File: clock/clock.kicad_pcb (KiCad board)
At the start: 2 copper layers, 176.8 x 81.3 mm, 285 parts, among them P101 CONN_01X03, P102 CONN_FAN_PWM, P103 XG4A-1631, P301 MCRF, Q201 MMBT3904, U201 PCA9306, U202 DAC8830, U203 LMV722, U204 LTC2990, U205 LP3853, U206 NC7SZ125, U207 NC7SZ125, U301 Adafruit746, U302 MIC5225, U303 PA6H, U401 74LVC541, U501 TPS56428, U502 TPS56428, U503 TPS56428, U601 ADT7410, U602 DS3231, U603 ADT7410, Y201 FVXO-HC53, Y202 CX210

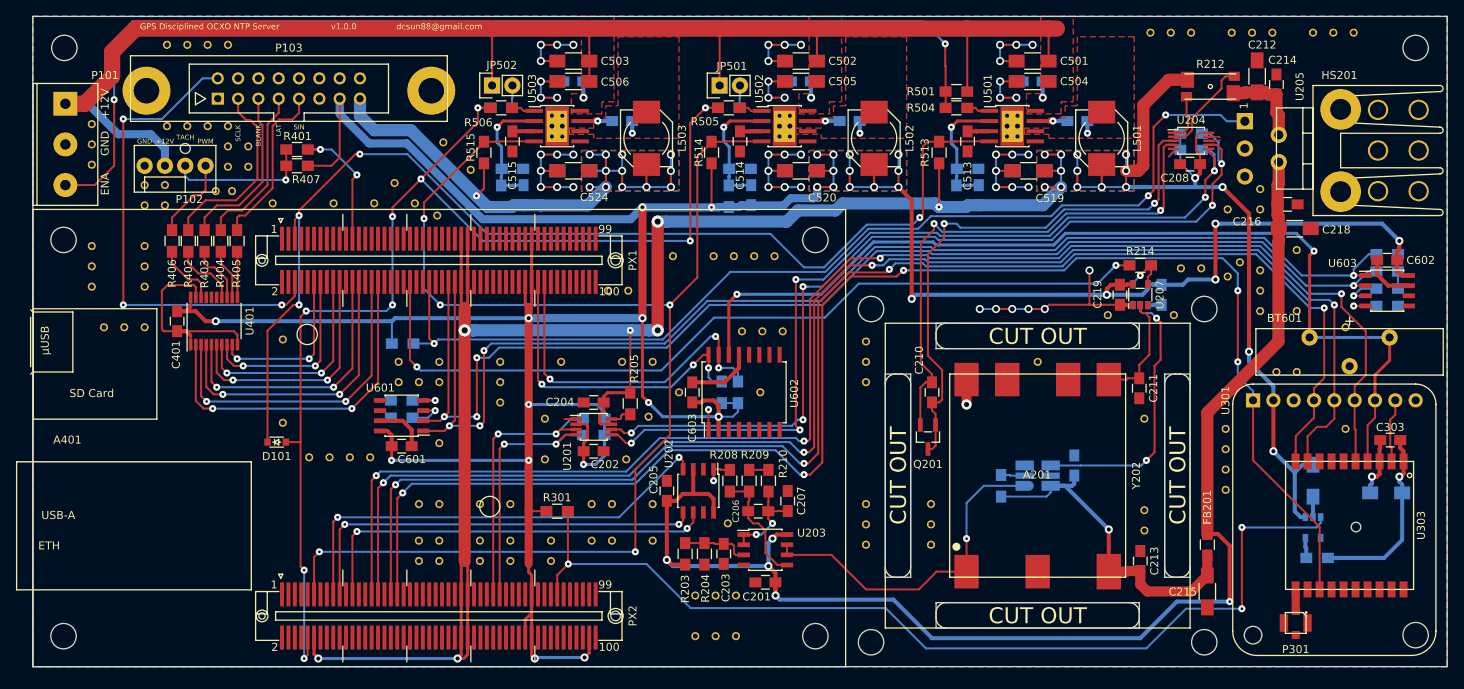
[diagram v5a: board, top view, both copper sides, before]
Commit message: Hide value in stitching via. Reduce width of display board by 10 mils.
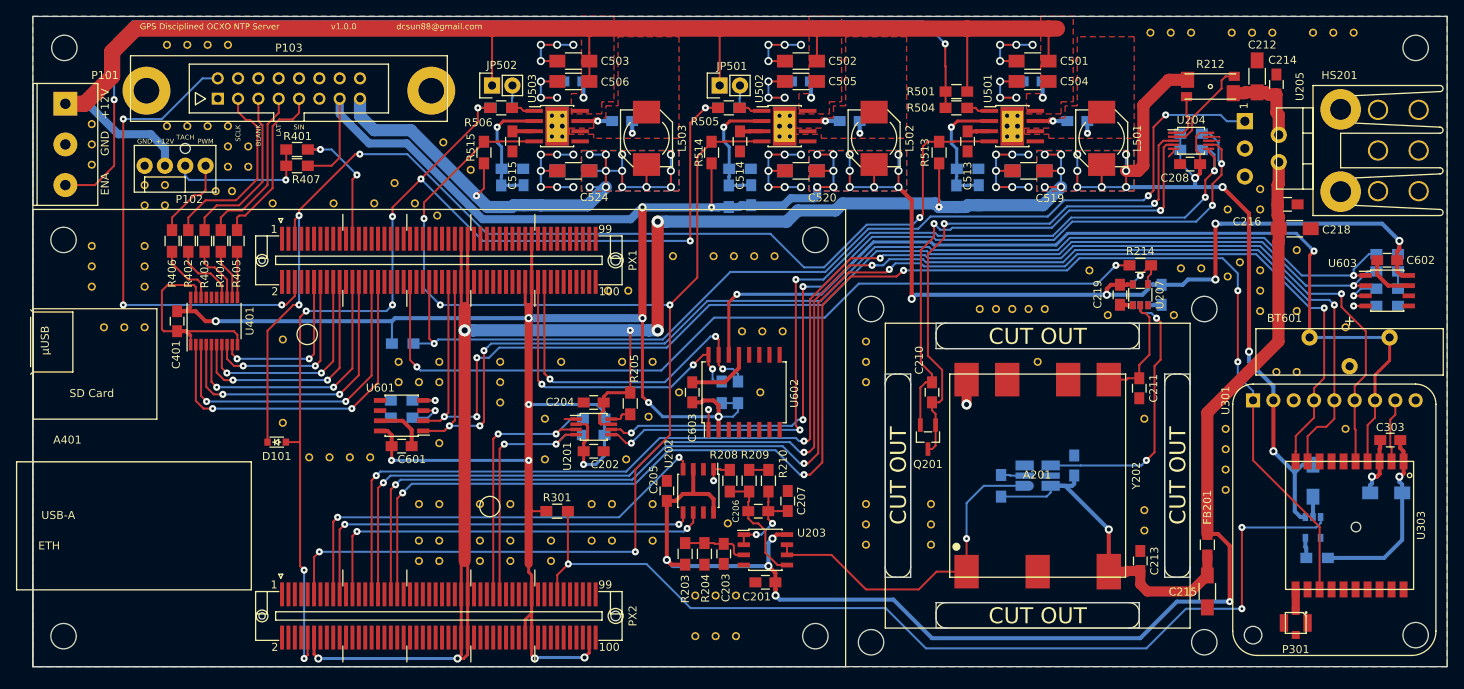
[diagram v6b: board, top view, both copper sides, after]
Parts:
- removed the REF** at (358.6, 186.9)
- removed the REF** at (358.6, 176.8)
- removed the REF** at (363.7, 176.8)
- removed the REF** at (363.7, 181.9)
- removed the REF** at (358.6, 181.9)
- removed the REF** at (363.7, 186.9)
- added REF**: Stitching_Via_40x24mil, local:Stitching_Via_40x24mil, F.Cu at (317.0, 201.7)
- added REF**: Stitching_Via_100x80mil, local:Stitching_Via_100x80mil, F.Cu at (363.7, 186.9)
- added REF**: Stitching_Via_100x80mil, local:Stitching_Via_100x80mil, F.Cu at (363.7, 176.8)
- added REF**: Stitching_Via_100x80mil, local:Stitching_Via_100x80mil, F.Cu at (363.7, 181.9)
- added REF**: Stitching_Via_40x24mil, local:Stitching_Via_40x24mil, F.Cu at (308.9, 201.7)
- added REF**: Stitching_Via_40x24mil, local:Stitching_Via_40x24mil, F.Cu at (310.9, 201.7)
- added REF**: Stitching_Via_40x24mil, local:Stitching_Via_40x24mil, F.Cu at (312.9, 201.7)
- added REF**: Stitching_Via_40x24mil, local:Stitching_Via_40x24mil, F.Cu at (315.0, 201.7)
- added REF**: Stitching_Via_40x24mil, local:Stitching_Via_40x24mil, F.Cu at (322.6, 196.9)
- added REF**: Stitching_Via_100x80mil, local:Stitching_Via_100x80mil, F.Cu at (358.6, 176.8)
- added REF**: Stitching_Via_100x80mil, local:Stitching_Via_100x80mil, F.Cu at (358.6, 181.9)
- added REF**: Stitching_Via_100x80mil, local:Stitching_Via_100x80mil, F.Cu at (358.6, 186.9)
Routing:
- net GND: track 174.3 -> 152.3 mm, vias 50 -> 44

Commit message: Lock all the stitching vias. Remove FVXO alternate to OCXO.
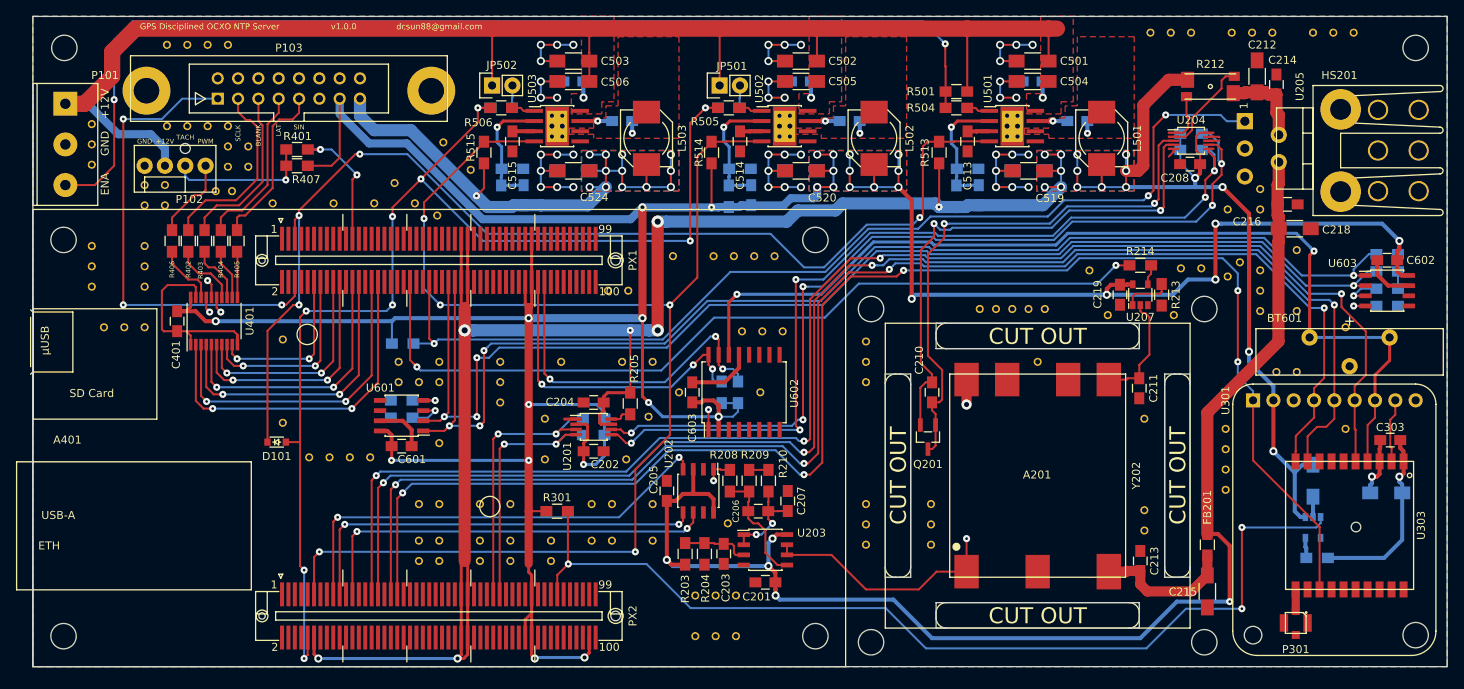
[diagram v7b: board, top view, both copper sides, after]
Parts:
- removed C209, C217: 0.1uF, Capacitors_SMD:C_0805_HandSoldering
- removed U206: NC7SZ125, local:SOT-23-5_1.6x2.9mm_Pitch0.95mm
- removed Y201: FVXO-HC53, local:FVXO_HandSoldering
- R213: value 100K -> 10.0K; moved to F.Cu
- moved R213 31.2 mm to (331.6, 199.9), turned to 270 degrees
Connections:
- P103 pad 1: GND -> /microzed/~CARRIER_SRST~
- P103 pad 2: /microzed/~CARRIER_SRST~ -> GND
- R213 pad 1: /ocxo/FILT_VXO -> /ocxo/BUF_ENA
- R213 pad 2: /ocxo/VCXO_ENA -> GND
- U207 pad 1: GND -> /ocxo/BUF_ENA
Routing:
- net /ocxo/VCXO_10M: track 34.1 -> 0.00 mm, vias 2 -> 0
- net /ocxo/FILT_VXO: track 42.6 -> 17.7 mm, vias 1 -> 0
- net /ocxo/VC: track 42.8 -> 30.6 mm
- net /ocxo/BUF_ENA: track 0.00 -> 5.95 mm
- net GND: track 152.3 -> 148.9 mm
- net /ocxo/BUF_10M: track 5.94 -> 2.65 mm, vias 1 -> 0
- net /ocxo/VCXO_ENA: track 2.98 -> 0.00 mm
- net Net-(U401-Pad16): track 0.00 -> 2.31 mm, vias 0 -> 1
- net Net-(U401-Pad15): track 0.00 -> 2.04 mm, vias 0 -> 1
- net Net-(U401-Pad17): track 0.00 -> 2.00 mm, vias 0 -> 1
- net /microzed/~CARRIER_SRST~: track 60.8 -> 59.8 mm
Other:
- rule trace_min: 0.006 -> 0.1524
- rule via_min_size: 0.027 -> 0.6858

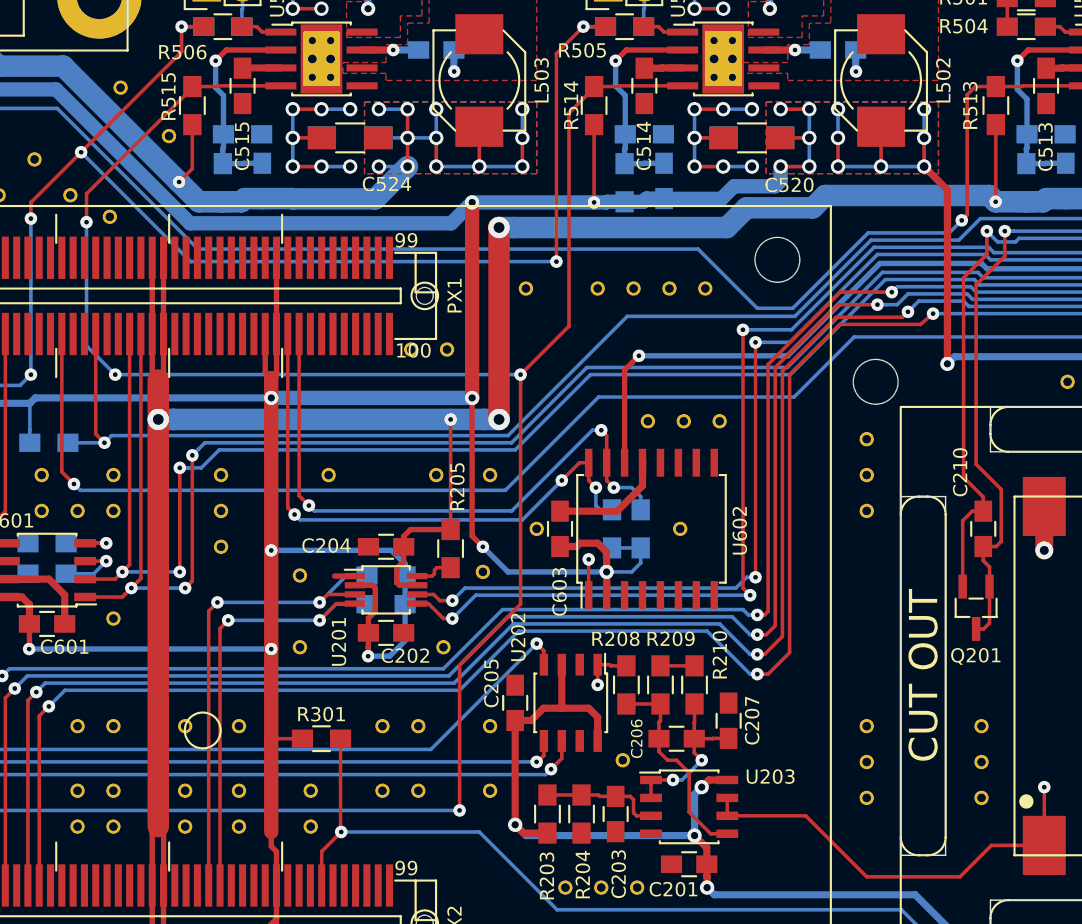
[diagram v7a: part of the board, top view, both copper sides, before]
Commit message: Rename gerbers for kicad 4.0.
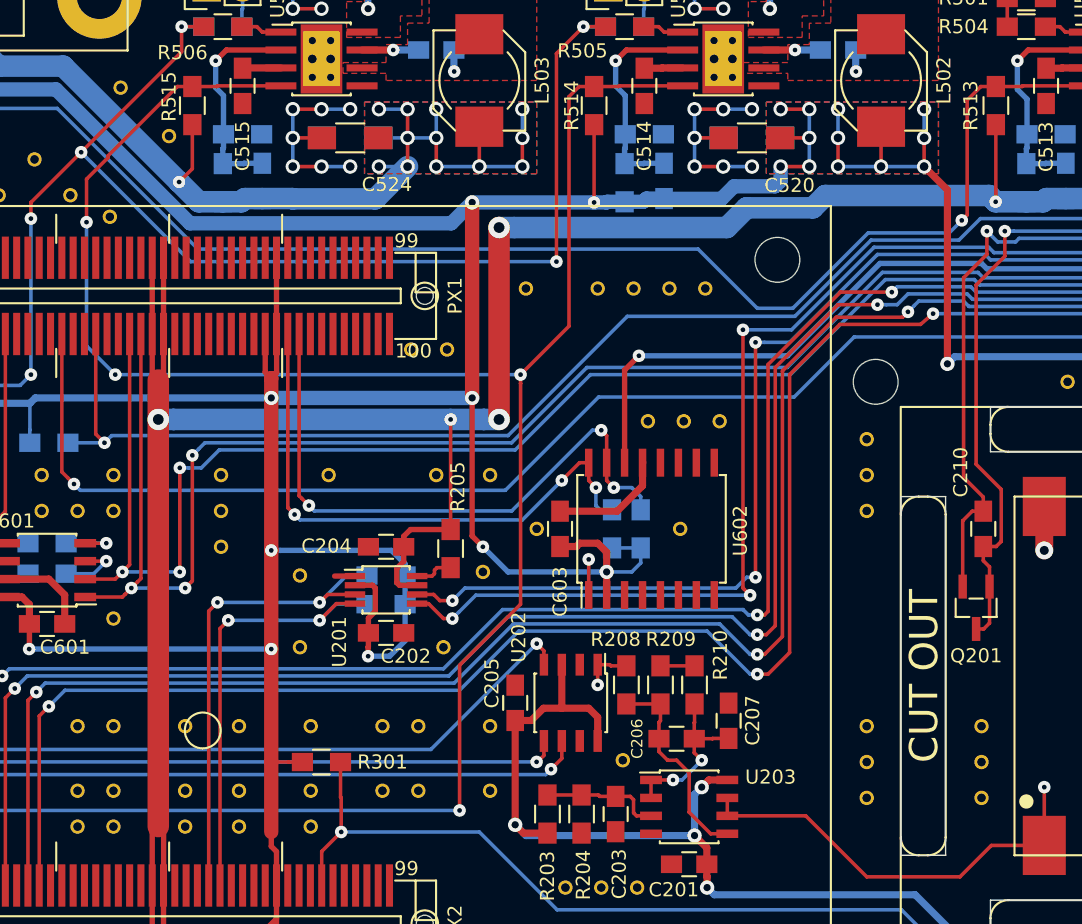
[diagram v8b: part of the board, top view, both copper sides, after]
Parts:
- added REF**: Stitching_Via_40x24mil, local:Stitching_Via_40x24mil, F.Cu at (255.3, 226.1)
- moved R301 1.65 mm to (256.0, 228.6)
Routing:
- net /gps/ENA: track 122.6 -> 120.9 mm
- net /power/+3.0V_PG: track 165.9 -> 167.2 mm
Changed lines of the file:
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@@
-(kicad_pcb (version 4) (host pcbnew "(2015-09-12 BZR 6188)-product")
+(kicad_pcb (version 4) (host pcbnew "(2015-12-09 BZR 6195)-product")
   (general
-    (links 551)
+    (links 552)
     (no_connects 0)
     (area 186.108 163.286 373.199858 246.709001)
     (thickness 1.6)
     (drawings 69)
-    (tracks 1493)
+    (tracks 1497)
     (zones 0)
-    (modules 287)
+    (modules 288)
     (nets 233)
   )
@@
   )
   (module local:Stitching_Via_40x24mil locked (layer F.Cu)
+    (at 255.27 226.06)
+    (fp_text reference REF** (at 0 1.778) (layer F.SilkS) hide
+      (effects (font (size 1 1) (thickness 0.15)))
+    )
+    (fp_text value Stitching_Via_40x24mil (at 0 -1.524) (layer F.Fab) hide
+      (effects (font (size 1 1) (thickness 0.15)))
+    )
+    (pad ~ thru_hole circle (at 0 0) (size 1.016 1.016) (drill 0.6096) (layers *.Cu *.Mask)
+      (net 2 GND) (zone_connect 2))
+  )
+  (module local:Stitching_Via_40x24mil locked (layer F.Cu)
     (at 316.992 201.676)
     (fp_text reference REF** (at 0 1.778) (layer F.SilkS) hide
@@
   )
   (module Resistors_SMD:R_0805_HandSoldering (layer F.Cu)
-    (at 256.032 226.949)
+    (at 256.032 228.6)
     (descr "Resistor SMD 0805, hand soldering")
     (tags "resistor 0805")
     (attr smd)
-    (fp_text reference R301 (at 0 -1.7018) (layer F.SilkS)
+    (fp_text reference R301 (at 4.318 0) (layer F.SilkS)
       (effects (font (size 1 1) (thickness 0.15)))
     )
@@
   (segment (start 237.851 216.769) (end 237.851 218.821) (width 0.508) (layer F.Cu) (net 2) (status 20))
   (segment (start 236.728 215.646) (end 237.851 216.769) (width 0.508) (layer F.Cu) (net 2))
+  (segment (start 254.682 228.6) (end 253.678 228.6) (width 0.254) (layer F.Cu) (net 3))
+  (segment (start 253.678 228.6) (end 252.476 228.6) (width 0.254) (layer F.Cu) (net 3))
+  (segment (start 252.476 233.553) (end 252.476 228.6) (width 1.016) (layer F.Cu) (net 3))
+  (segment (start 252.476 228.6) (end 252.476 220.598978) (width 1.016) (layer F.Cu) (net 3))
   (segment (start 324.739 199.898) (end 332.994 199.898) (width 0.508) (layer B.Cu) (net 3))
   (segment (start 332.994 199.898) (end 334.899 197.993) (width 0.508) (layer B.Cu) (net 3))
@@
   (segment (start 252.857 201.041) (end 252.857 198.3025) (width 0.381) (layer F.Cu) (net 3))
   (segment (start 252.857 198.3025) (end 252.8472 198.2927) (width 0.381) (layer F.Cu) (net 3))
-  (segment (start 252.476 226.949) (end 252.476 220.598978) (width 1.016) (layer F.Cu) (net 3))
-  (segment (start 254.682 226.949) (end 252.476 226.949) (width 0.254) (layer F.Cu) (net 3))
-  (segment (start 252.476 233.553) (end 252.476 226.949) (width 1.016) (layer F.Cu) (net 3))
   (segment (start 259.334 221.107) (end 259.334 220.472) (width 0.381) (layer F.Cu) (net 3))
   (segment (start 259.334 220.472) (end 259.354 220.452) (width 0.381) (layer F.Cu) (net 3))
@@
   (segment (start 238.061507 208.470501) (end 238.506006 208.915) (width 0.254) (layer F.Cu) (net 20))
   (via (at 238.506006 208.915) (size 0.889) (drill 0.3302) (layers F.Cu B.Cu) (net 20))
+  (segment (start 257.382 228.6) (end 257.382 231.093) (width 0.254) (layer F.Cu) (net 21))
+  (segment (start 257.382 231.093) (end 257.429 231.14) (width 0.254) (layer F.Cu) (net 21))
+  (segment (start 257.429 231.14) (end 257.429 233.553) (width 0.254) (layer F.Cu) (net 21))
   (segment (start 257.429 233.553) (end 256.0472 234.9348) (width 0.254) (layer F.Cu) (net 21))
   (segment (start 256.0472 234.9348) (end 256.0472 237.3427) (width 0.254) (layer F.Cu) (net 21) (status 20))
-  (segment (start 257.382 226.949) (end 257.382 233.506) (width 0.254) (layer F.Cu) (net 21) (status 10))
   (segment (start 267.208 233.553) (end 272.716699 239.061699) (width 0.254) (layer B.Cu) (net 21))
   (segment (start 257.429 233.553) (end 267.208 233.553) (width 0.254) (layer B.Cu) (net 21))
   (via (at 257.429 233.553) (size 0.889) (drill 0.3302) (layers F.Cu B.Cu) (net 21))
-  (segment (start 257.382 233.506) (end 257.429 233.553) (width 0.254) (layer F.Cu) (net 21))
   (segment (start 341.63 239.141) (end 334.645 239.141) (width 0.254) (layer B.Cu) (net 21))
   (segment (start 334.645 239.141) (end 329.692 244.094) (width 0.254) (layer B.Cu) (net 21))
@@
   (segment (start 251.46 176.53) (end 250.397 176.53) (width 0.254) (layer F.Cu) (net 38) (status 20))
   (segment (start 251.841 176.911) (end 251.46 176.53) (width 0.254) (layer F.Cu) (net 38))
+  (segment (start 303.784 180.768) (end 302.721 180.768) (width 0.254) (layer F.Cu) (net 39))
+  (segment (start 302.721 180.768) (end 301.752 181.737) (width 0.254) (layer F.Cu) (net 39))
+  (segment (start 301.752 181.737) (end 301.752 189.865) (width 0.254) (layer F.Cu) (net 39))
+  (segment (start 301.752 189.865) (end 301.371 190.246) (width 0.254) (layer F.Cu) (net 39))
   (segment (start 223.774 189.992012) (end 223.774 201.168) (width 0.254) (layer B.Cu) (net 39))
   (segment (start 301.371 190.246) (end 300.482 191.135) (width 0.254) (layer B.Cu) (net 39))
@@
   (segment (start 282.702021 192.278021) (end 247.281772 192.278021) (width 0.254) (layer B.Cu) (net 39))
   (segment (start 237.321792 182.318041) (end 231.372924 182.318041) (width 0.254) (layer B.Cu) (net 39))
-  (segment (start 303.784 180.768) (end 302.34 180.768) (width 0.254) (layer F.Cu) (net 39))
-  (segment (start 302.34 180.768) (end 301.752 181.356) (width 0.254) (layer F.Cu) (net 39))
-  (segment (start 301.752 181.356) (end 301.752 189.865) (width 0.254) (layer F.Cu) (net 39))
-  (segment (start 301.752 189.865) (end 301.371 190.246) (width 0.254) (layer F.Cu) (net 39))
   (segment (start 223.774 201.168) (end 223.0628 201.168) (width 0.254) (layer F.Cu) (net 39))
   (segment (start 223.0628 201.168) (end 219.83 204.4008) (width 0.254) (layer F.Cu) (net 39))
@@
   (segment (start 305.642 180.768) (end 303.784 180.768) (width 0.254) (layer F.Cu) (net 39) (status 20))
   (segment (start 310.053 180.721) (end 305.689 180.721) (width 0.254) (layer F.Cu) (net 39) (status 10))
+  (segment (start 246.888 180.768) (end 245.825 180.768) (width 0.254) (layer F.Cu) (net 40))
+  (segment (start 245.825 180.768) (end 240.919 185.674) (width 0.254) (layer F.Cu) (net 40))
+  (segment (start 240.919 185.674) (end 240.919 185.801) (width 0.254) (layer F.Cu) (net 40))
+  (segment (start 240.919 185.801) (end 239.395 187.325) (width 0.254) (layer F.Cu) (net 40))
+  (segment (start 239.395 187.325) (end 239.395 190.373) (width 0.254) (layer F.Cu) (net 40))
+  (segment (start 275.336 180.768) (end 274.273 180.768) (width 0.254) (layer F.Cu) (net 40))
+  (segment (start 274.273 180.768) (end 273.558 181.483) (width 0.254) (layer F.Cu) (net 40))
+  (segment (start 273.558 181.483) (end 273.558 197.739004) (width 0.254) (layer F.Cu) (net 40))
+  (segment (start 273.558 197.739004) (end 270.129004 201.168) (width 0.254) (layer F.Cu) (net 40))
   (segment (start 239.395 199.135998) (end 241.427002 201.168) (width 0.254) (layer B.Cu) (net 40))
   (segment (start 239.395 190.373) (end 239.395 199.135998) (width 0.254) (layer B.Cu) (net 40))
@@
   (segment (start 270.129004 201.168) (end 270.129004 201.796617) (width 0.254) (layer F.Cu) (net 40))
   (segment (start 270.129004 201.796617) (end 270.129 201.796621) (width 0.254) (layer F.Cu) (net 40))
-  (segment (start 273.558 197.739004) (end 270.129004 201.168) (width 0.254) (layer F.Cu) (net 40))
-  (segment (start 273.558 182.646) (end 273.558 197.739004) (width 0.254) (layer F.Cu) (net 40))
-  (segment (start 275.336 180.868) (end 273.558 182.646) (width 0.254) (layer F.Cu) (net 40) (status 10))
-  (segment (start 275.336 180.768) (end 275.336 180.868) (width 0.254) (layer F.Cu) (net 40) (status 30))
   (via (at 270.129004 201.168) (size 0.889) (drill 0.3302) (layers F.Cu B.Cu) (net 40))
-  (segment (start 239.395 188.361) (end 239.395 190.373) (width 0.254) (layer F.Cu) (net 40))
-  (segment (start 246.888 180.868) (end 239.395 188.361) (width 0.254) (layer F.Cu) (net 40) (status 10))
-  (segment (start 246.888 180.768) (end 246.888 180.868) (width 0.254) (layer F.Cu) (net 40) (status 30))
   (via (at 239.395 190.373) (size 0.889) (drill 0.3302) (layers F.Cu B.Cu) (net 40))
   (segment (start 277.114 180.721) (end 277.067 180.768) (width 0.254) (layer F.Cu) (net 40))
